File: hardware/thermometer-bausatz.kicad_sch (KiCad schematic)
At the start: 25 parts, among them J1 TEST_1P, J2 TEST_1P, J3 UPDI, U1 ATTINY24A-SSU, U2 MCP9700AT-E_TT

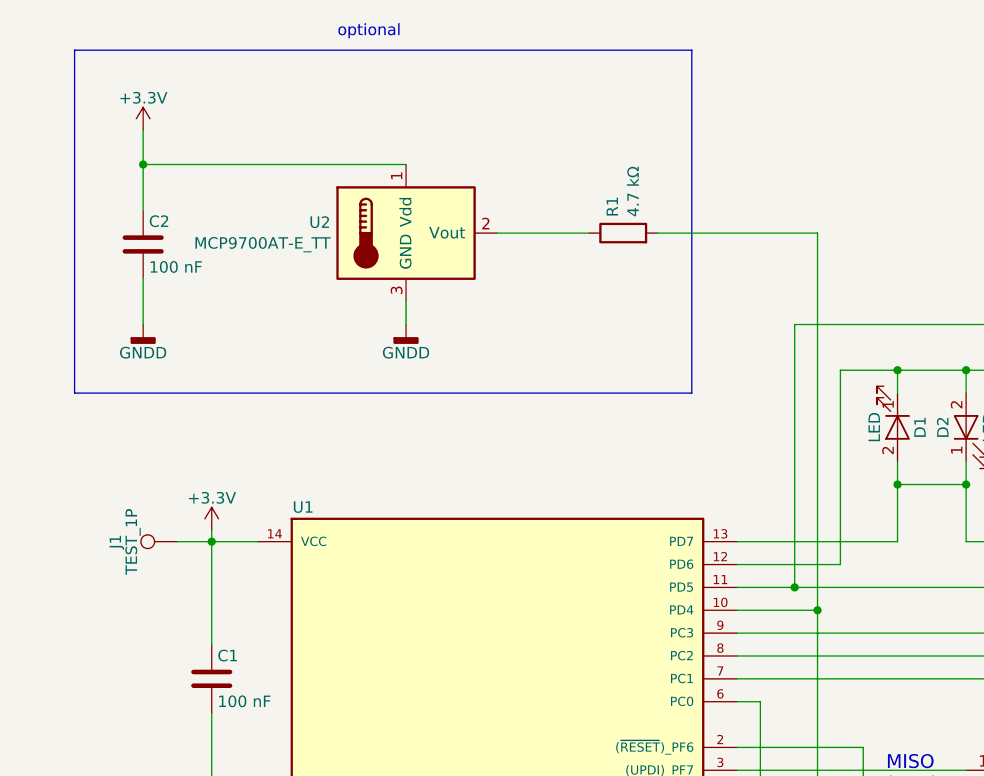
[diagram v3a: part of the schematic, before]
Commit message: Remove external temperature sensor
The external sensor was initially designed as an option to allow for a
more accurate temperature sensor. To save part costs, it has never
actually been implemented.

With the AVRxEB, the internal temperature sensor comes pre-calibrated
(through fuse values), so it is safe to get rid of that idea
entirely.
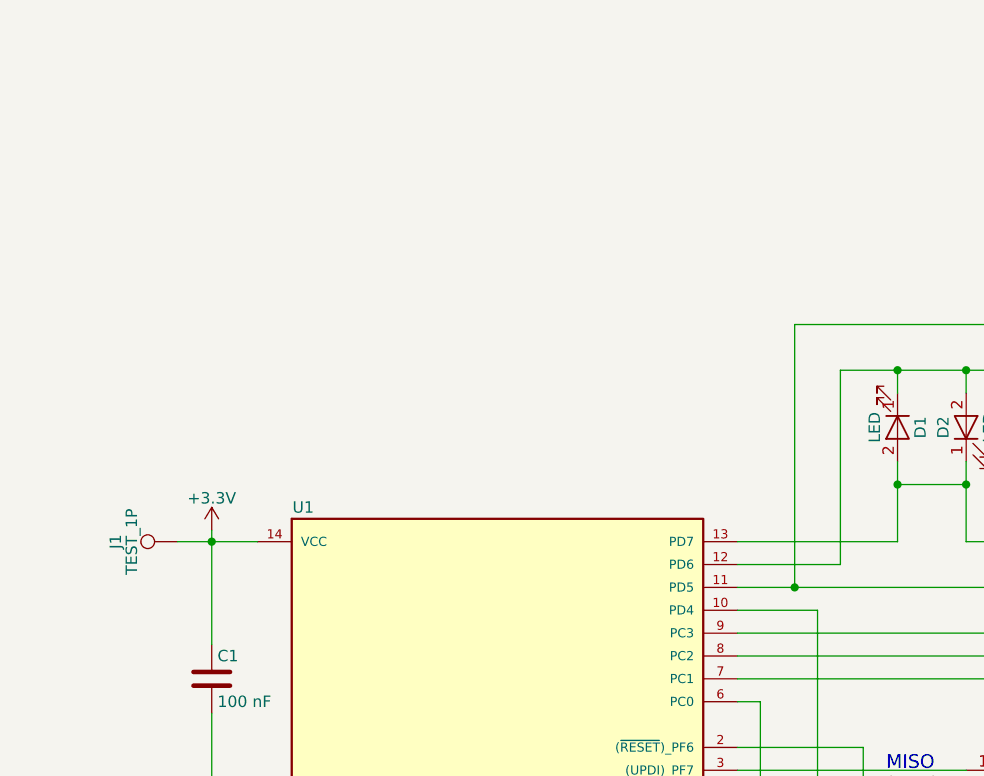
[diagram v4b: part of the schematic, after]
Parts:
- removed C2: 100 nF, Capacitor_SMD:C_0805_2012Metric_Pad1.18x1.45mm_HandSolder, symbol thermometer-bausatz-rescue:C-device
- removed R1: 4.7 kΩ, Resistor_SMD:R_0805_2012Metric_Pad1.20x1.40mm_HandSolder, symbol thermometer-bausatz-rescue:R-device
- removed U2: MCP9700AT-E_TT, Package_TO_SOT_SMD:SOT-23, symbol thermometer-bausatz-rescue:MCP9700AT-E_TT-sensors
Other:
- note removed: "optional"
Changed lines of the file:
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@@
     (company "DARC OV „Pentacon Dresden“")
   )
-  (junction (at 55.88 45.72) (diameter 0) (color 0 0 0 0)
-  )
   (junction (at 193.04 87.63) (diameter 0) (color 0 0 0 0)
   )
@@
   (junction (at 139.7 68.58) (diameter 0) (color 0 0 0 0)
   )
-  (junction (at 130.81 95.25) (diameter 0) (color 0 0 0 0)
-  )
   (junction (at 208.28 81.28) (diameter 0) (color 0 0 0 0)
   )
@@
     (stroke (width 0) (type default))
   )
-  (polyline (pts (xy 48.26 33.02) (xy 48.26 71.12))
-    (stroke (width 0) (type default))
-  )
-  (polyline (pts (xy 116.84 71.12) (xy 116.84 33.02))
-    (stroke (width 0) (type default))
-  )
-  (wire (pts (xy 95.25 53.34) (xy 105.41 53.34))
-    (stroke (width 0) (type default))
-  )
   (wire (pts (xy 63.5 118.11) (xy 68.58 118.11))
     (stroke (width 0) (type default))
@@
     (stroke (width 0) (type default))
   )
-  (wire (pts (xy 55.88 63.5) (xy 55.88 58.42))
-    (stroke (width 0) (type default))
-  )
   (wire (pts (xy 121.92 95.25) (xy 130.81 95.25))
     (stroke (width 0) (type default))
@@
     (stroke (width 0) (type default))
   )
-  (wire (pts (xy 130.81 53.34) (xy 130.81 95.25))
-    (stroke (width 0) (type default))
-  )
   (wire (pts (xy 121.92 118.11) (xy 133.35 118.11))
     (stroke (width 0) (type default))
   )
-  (wire (pts (xy 85.09 60.96) (xy 85.09 63.5))
-    (stroke (width 0) (type default))
-  )
   (wire (pts (xy 215.9 68.58) (xy 231.14 68.58))
     (stroke (width 0) (type default))
@@
     (stroke (width 0) (type default))
   )
-  (wire (pts (xy 55.88 45.72) (xy 55.88 41.91))
-    (stroke (width 0) (type default))
-  )
   (wire (pts (xy 63.5 86.36) (xy 63.5 87.63))
     (stroke (width 0) (type default))
@@
     (stroke (width 0) (type default))
   )
-  (polyline (pts (xy 116.84 33.02) (xy 48.26 33.02))
-    (stroke (width 0) (type default))
-  )
   (wire (pts (xy 170.18 81.28) (xy 177.8 81.28))
     (stroke (width 0) (type default))
   )
-  (wire (pts (xy 113.03 53.34) (xy 130.81 53.34))
-    (stroke (width 0) (type default))
-  )
   (wire (pts (xy 154.94 68.58) (xy 154.94 71.12))
     (stroke (width 0) (type default))
@@
     (stroke (width 0) (type default))
   )
-  (wire (pts (xy 55.88 45.72) (xy 85.09 45.72))
-    (stroke (width 0) (type default))
-  )
   (wire (pts (xy 124.46 105.41) (xy 124.46 124.46))
     (stroke (width 0) (type default))
@@
     (stroke (width 0) (type default))
   )
-  (wire (pts (xy 55.88 50.8) (xy 55.88 45.72))
-    (stroke (width 0) (type default))
-  )
   (wire (pts (xy 59.69 87.63) (xy 63.5 87.63))
-    (stroke (width 0) (type default))
-  )
-  (polyline (pts (xy 48.26 71.12) (xy 116.84 71.12))
     (stroke (width 0) (type default))
   )
@@
     (effects (font (size 1.27 1.27)) (justify left bottom))
   )
-  (text "optional" (at 77.47 31.75 0)
-    (effects (font (size 1.27 1.27)) (justify left bottom))
-  )
   (text "MISO\n(SCK)\n(~{RST})" (at 138.43 118.11 0)
     (effects (font (size 1.524 1.524)) (justify left bottom))
@@
         )
       )
-    )
-  )
-  (symbol (lib_id "thermometer-bausatz-rescue:MCP9700AT-E_TT-sensors") (at 85.09 53.34 0) (unit 1)
-    (in_bom yes) (on_board yes) (dnp no)
-    (property "Reference" "U2" (at 76.708 52.1716 0)
-      (effects (font (size 1.27 1.27)) (justify right))
-    )
-    (property "Value" "MCP9700AT-E_TT" (at 76.708 54.483 0)
-      (effects (font (size 1.27 1.27)) (justify right))
-    )
-    (property "Footprint" "Package_TO_SOT_SMD:SOT-23" (at 85.09 63.5 0)
-      (effects (font (size 1.27 1.27)) hide)
-    )
-    (property "Datasheet" "" (at 81.28 46.99 0)
-      (effects (font (size 1.27 1.27)) hide)
-    )
-    (pin "1")
-    (pin "2")
-    (pin "3")
-    (instances
-      (project "thermometer-bausatz"
-        (path "/b629b0f3-9b5f-44da-8346-e958d88e091c"
-          (reference "U2") (unit 1)
-        )
-      )
-    )
-  )
-  (symbol (lib_id "thermometer-bausatz-rescue:R-device") (at 109.22 53.34 90) (unit 1)
-    (in_bom yes) (on_board yes) (dnp no)
-    (property "Reference" "R1" (at 108.0516 51.562 0)
-      (effects (font (size 1.27 1.27)) (justify left))
-    )
-    (property "Value" "4.7 kΩ" (at 110.363 51.562 0)
-      (effects (font (size 1.27 1.27)) (justify left))
-    )
-    (property "Footprint" "Resistor_SMD:R_0805_2012Metric_Pad1.20x1.40mm_HandSolder" (at 109.22 55.118 90)
-      (effects (font (size 1.27 1.27)) hide)
-    )
-    (property "Datasheet" "" (at 109.22 53.34 0)
-      (effects (font (size 1.27 1.27)) hide)
-    )
-    (pin "1")
-    (pin "2")
-    (instances
-      (project "thermometer-bausatz"
-        (path "/b629b0f3-9b5f-44da-8346-e958d88e091c"
-          (reference "R1") (unit 1)
-        )
-      )
-    )
-  )
-  (symbol (lib_id "thermometer-bausatz-rescue:C-device") (at 55.88 54.61 0) (unit 1)
-    (in_bom yes) (on_board yes) (dnp no)
-    (property "Reference" "C2" (at 56.515 52.07 0)
-      (effects (font (size 1.27 1.27)) (justify left))
-    )
-    (property "Value" "100 nF" (at 56.515 57.15 0)
-      (effects (font (size 1.27 1.27)) (justify left))
-    )
-    (property "Footprint" "Capacitor_SMD:C_0805_2012Metric_Pad1.18x1.45mm_HandSolder" (at 56.8452 58.42 0)
-      (effects (font (size 1.27 1.27)) hide)
-    )
-    (property "Datasheet" "" (at 55.88 54.61 0)
-      (effects (font (size 1.27 1.27)) hide)
-    )
-    (pin "1")
-    (pin "2")
-    (instances
-      (project "thermometer-bausatz"
-        (path "/b629b0f3-9b5f-44da-8346-e958d88e091c"
-          (reference "C2") (unit 1)
-        )
-      )
-    )
-  )
-  (symbol (lib_id "thermometer-bausatz-rescue:+3.3V-power") (at 55.88 41.91 0) (unit 1)
-    (in_bom yes) (on_board yes) (dnp no)
-    (property "Reference" "#PWR08" (at 55.88 45.72 0)
-      (effects (font (size 1.27 1.27)) hide)
-    )
-    (property "Value" "+3.3V" (at 55.88 38.354 0)
-      (effects (font (size 1.27 1.27)))
-    )
-    (property "Footprint" "" (at 55.88 41.91 0)
-      (effects (font (size 1.27 1.27)) hide)
-    )
-    (property "Datasheet" "" (at 55.88 41.91 0)
-      (effects (font (size 1.27 1.27)) hide)
-    )
-    (pin "1")
-    (instances
-      (project "thermometer-bausatz"
-        (path "/b629b0f3-9b5f-44da-8346-e958d88e091c"
-          (reference "#PWR08") (unit 1)
-        )
-      )
-    )
-  )
-  (symbol (lib_id "power:GNDD") (at 55.88 63.5 0) (unit 1)
-    (in_bom yes) (on_board yes) (dnp no)
-    (property "Reference" "#PWR09" (at 55.88 69.85 0)
-      (effects (font (size 1.27 1.27)) hide)
-    )
-    (property "Value" "GNDD" (at 55.88 66.675 0)
-      (effects (font (size 1.27 1.27)))
-    )
-    (property "Footprint" "" (at 55.88 63.5 0)
-      (effects (font (size 1.27 1.27)) hide)
-    )
-    (property "Datasheet" "" (at 55.88 63.5 0)
-      (effects (font (size 1.27 1.27)) hide)
-    )
-    (pin "1")
-    (instances
-      (project "thermometer-bausatz"
-        (path "/b629b0f3-9b5f-44da-8346-e958d88e091c"
-          (reference "#PWR09") (unit 1)
-        )
-      )
-    )
-  )
-  (symbol (lib_id "power:GNDD") (at 85.09 63.5 0) (unit 1)
-    (in_bom yes) (on_board yes) (dnp no)
-    (property "Reference" "#PWR010" (at 85.09 69.85 0)
-      (effects (font (size 1.27 1.27)) hide)
-    )
-    (property "Value" "GNDD" (at 85.09 66.675 0)
-      (effects (font (size 1.27 1.27)))
-    )
-    (property "Footprint" "" (at 85.09 63.5 0)
-      (effects (font (size 1.27 1.27)) hide)
-    )
-    (property "Datasheet" "" (at 85.09 63.5 0)
-      (effects (font (size 1.27 1.27)) hide)
-    )
-    (pin "1")
-    (instances
-      (project "thermometer-bausatz"
-        (path "/b629b0f3-9b5f-44da-8346-e958d88e091c"
-          (reference "#PWR010") (unit 1)
-        )
-      )

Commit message: Change MCU type to AVR16EB14-I/SL
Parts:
- U1: value ATTINY24A-SSU -> AVR16EB14-I/SL
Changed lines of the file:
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@@
       (effects (font (size 1.27 1.27)))
     )
-    (property "Value" "ATTINY24A-SSU" (at 111.76 121.92 0)
+    (property "Value" "AVR16EB14-I/SL" (at 111.76 121.92 0)
       (effects (font (size 1.27 1.27)))
     )
